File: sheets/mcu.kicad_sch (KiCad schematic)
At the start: 37 parts, among them SW1 SW_Nidec_CAS-120A1, SW2 SW_Push, U1 STM32H755ZIT6, Y1 25M, Y2 32k768

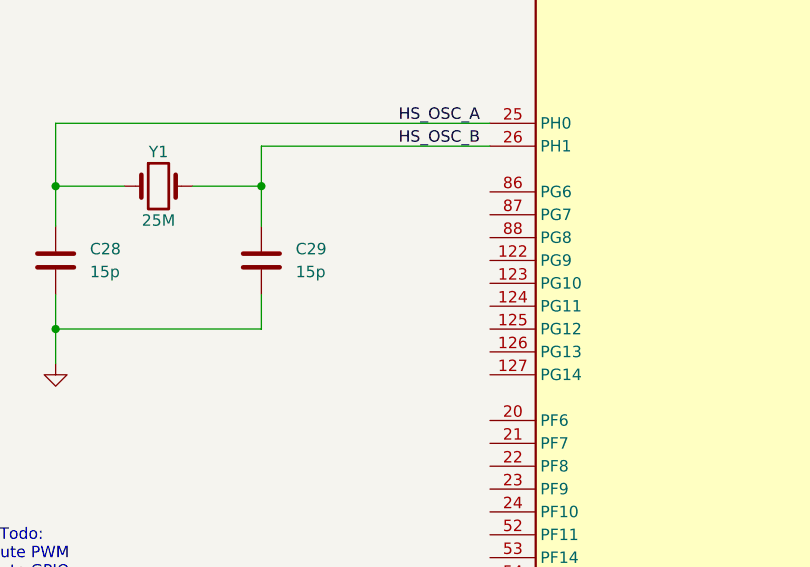
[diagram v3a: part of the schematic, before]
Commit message: assigned gpio pin to led (pg6)
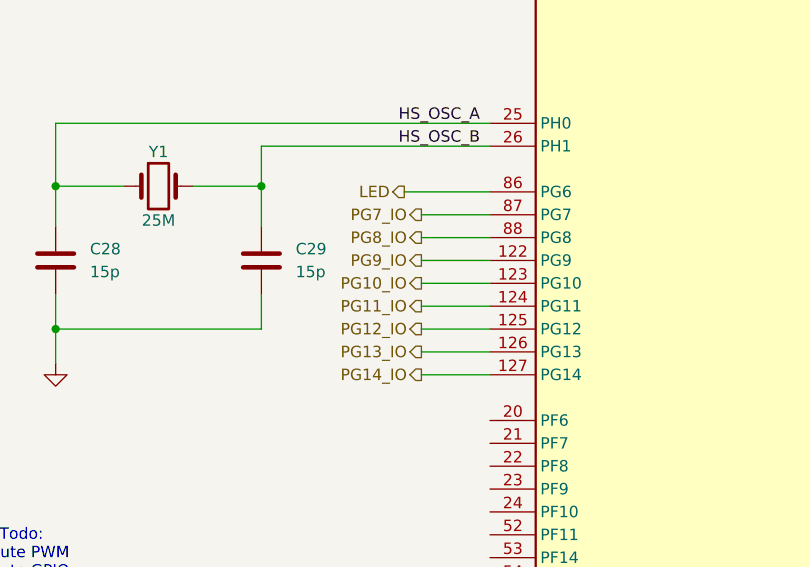
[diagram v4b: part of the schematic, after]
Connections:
- net PG9_IO: now reaches U1.122 (PG9)
- net PG10_IO: now reaches U1.123 (PG10)
- net PG11_IO: now reaches U1.124 (PG11)
- net PG12_IO: now reaches U1.125 (PG12)
- net PG13_IO: now reaches U1.126 (PG13)
- net PG14_IO: now reaches U1.127 (PG14)
- net LED: now reaches U1.86 (PG6)
- net PG7_IO: now reaches U1.87 (PG7)
- net PG8_IO: now reaches U1.88 (PG8)
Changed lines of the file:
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@@
 	(wire
 		(pts
+			(xy 257.81 111.76) (xy 265.43 111.76)
+		)
+		(stroke
+			(width 0)
+			(type default)
+		)
+	)
+	(wire
+		(pts
 			(xy 351.79 81.28) (xy 356.87 81.28)
 		)
@@
 	(wire
 		(pts
+			(xy 257.81 116.84) (xy 265.43 116.84)
+		)
+		(stroke
+			(width 0)
+			(type default)
+		)
+	)
+	(wire
+		(pts
 			(xy 129.54 82.55) (xy 132.08 82.55)
 		)
@@
 	(wire
 		(pts
+			(xy 257.81 121.92) (xy 265.43 121.92)
+		)
+		(stroke
+			(width 0)
+			(type default)
+		)
+	)
+	(wire
+		(pts
 			(xy 220.98 45.72) (xy 220.98 49.53)
 		)
@@
 	(wire
 		(pts
+			(xy 257.81 109.22) (xy 265.43 109.22)
+		)
+		(stroke
+			(width 0)
+			(type default)
+		)
+	)
+	(wire
+		(pts
 			(xy 351.79 142.24) (xy 366.395 142.24)
 		)
@@
 	(wire
 		(pts
+			(xy 257.81 119.38) (xy 265.43 119.38)
+		)
+		(stroke
+			(width 0)
+			(type default)
+		)
+	)
+	(wire
+		(pts
 			(xy 130.81 26.67) (xy 130.81 27.94)
 		)
@@
 	(wire
 		(pts
+			(xy 257.81 106.68) (xy 265.43 106.68)
+		)
+		(stroke
+			(width 0)
+			(type default)
+		)
+	)
+	(wire
+		(pts
 			(xy 109.22 82.55) (xy 109.22 86.36)
 		)
@@
 		)
 	)
+	(wire
+		(pts
+			(xy 257.81 124.46) (xy 265.43 124.46)
+		)
+		(stroke
+			(width 0)
+			(type default)
+		)
+	)
 	(bus
 		(pts
@@
 	(wire
 		(pts
+			(xy 257.81 114.3) (xy 265.43 114.3)
+		)
+		(stroke
+			(width 0)
+			(type default)
+		)
+	)
+	(wire
+		(pts
 			(xy 62.23 24.13) (xy 50.8 24.13)
 		)
@@
 	(wire
 		(pts
+			(xy 255.905 104.14) (xy 265.43 104.14)
+		)
+		(stroke
+			(width 0)
+			(type default)
+		)
+	)
+	(wire
+		(pts
 			(xy 109.22 82.55) (xy 111.76 82.55)
 		)
@@
 		)
 	)
+	(hierarchical_label "PG8_IO"
+		(shape output)
+		(at 257.81 109.22 180)
+		(effects
+			(font
+				(size 1.27 1.27)
+			)
+			(justify right)
+		)
+	)
 	(hierarchical_label "NEOM9N_EXTI0"
 		(shape input)
@@
 		)
 	)
+	(hierarchical_label "PG11_IO"
+		(shape output)
+		(at 257.81 116.84 180)
+		(effects
+			(font
+				(size 1.27 1.27)
+			)
+			(justify right)
+		)
+	)
 	(hierarchical_label "ADXL345{CS, SCLK, SDI, SDO, INT}"
 		(shape bidirectional)
@@
 		)
 	)
+	(hierarchical_label "PG10_IO"
+		(shape output)
+		(at 257.81 114.3 180)
+		(effects
+			(font
+				(size 1.27 1.27)
+			)
+			(justify right)
+		)
+	)
 	(hierarchical_label "LED_R"
 		(shape output)
@@
 		)
 	)
+	(hierarchical_label "LED"
+		(shape output)
+		(at 255.905 104.14 180)
+		(effects
+			(font
+				(size 1.27 1.27)
+			)
+			(justify right)
+		)
+	)
 	(hierarchical_label "SPARE_ADC1"
 		(shape input)
@@
 		)
 	)
+	(hierarchical_label "PG12_IO"
+		(shape output)
+		(at 257.81 119.38 180)
+		(effects
+			(font
+				(size 1.27 1.27)
+			)
+			(justify right)
+		)
+	)
 	(hierarchical_label "USB_D_P"
 		(shape bidirectional)
@@
 		)
 	)
+	(hierarchical_label "PG14_IO"
+		(shape output)
+		(at 257.81 124.46 180)
+		(effects
+			(font
+				(size 1.27 1.27)
+			)
+			(justify right)
+		)
+	)
+	(hierarchical_label "PG9_IO"
+		(shape output)
+		(at 257.81 111.76 180)
+		(effects
+			(font
+				(size 1.27 1.27)
+			)
+			(justify right)
+		)
+	)
 	(hierarchical_label "AIRBRAKE_POT1"
 		(shape input)
@@
 		)
 	)
+	(hierarchical_label "PG7_IO"
+		(shape output)
+		(at 257.81 106.68 180)
+		(effects
+			(font
+				(size 1.27 1.27)
+			)
+			(justify right)
+		)
+	)
+	(hierarchical_label "PG13_IO"
+		(shape output)
+		(at 257.81 121.92 180)
+		(effects
+			(font
+				(size 1.27 1.27)
+			)
+			(justify right)
+		)
+	)

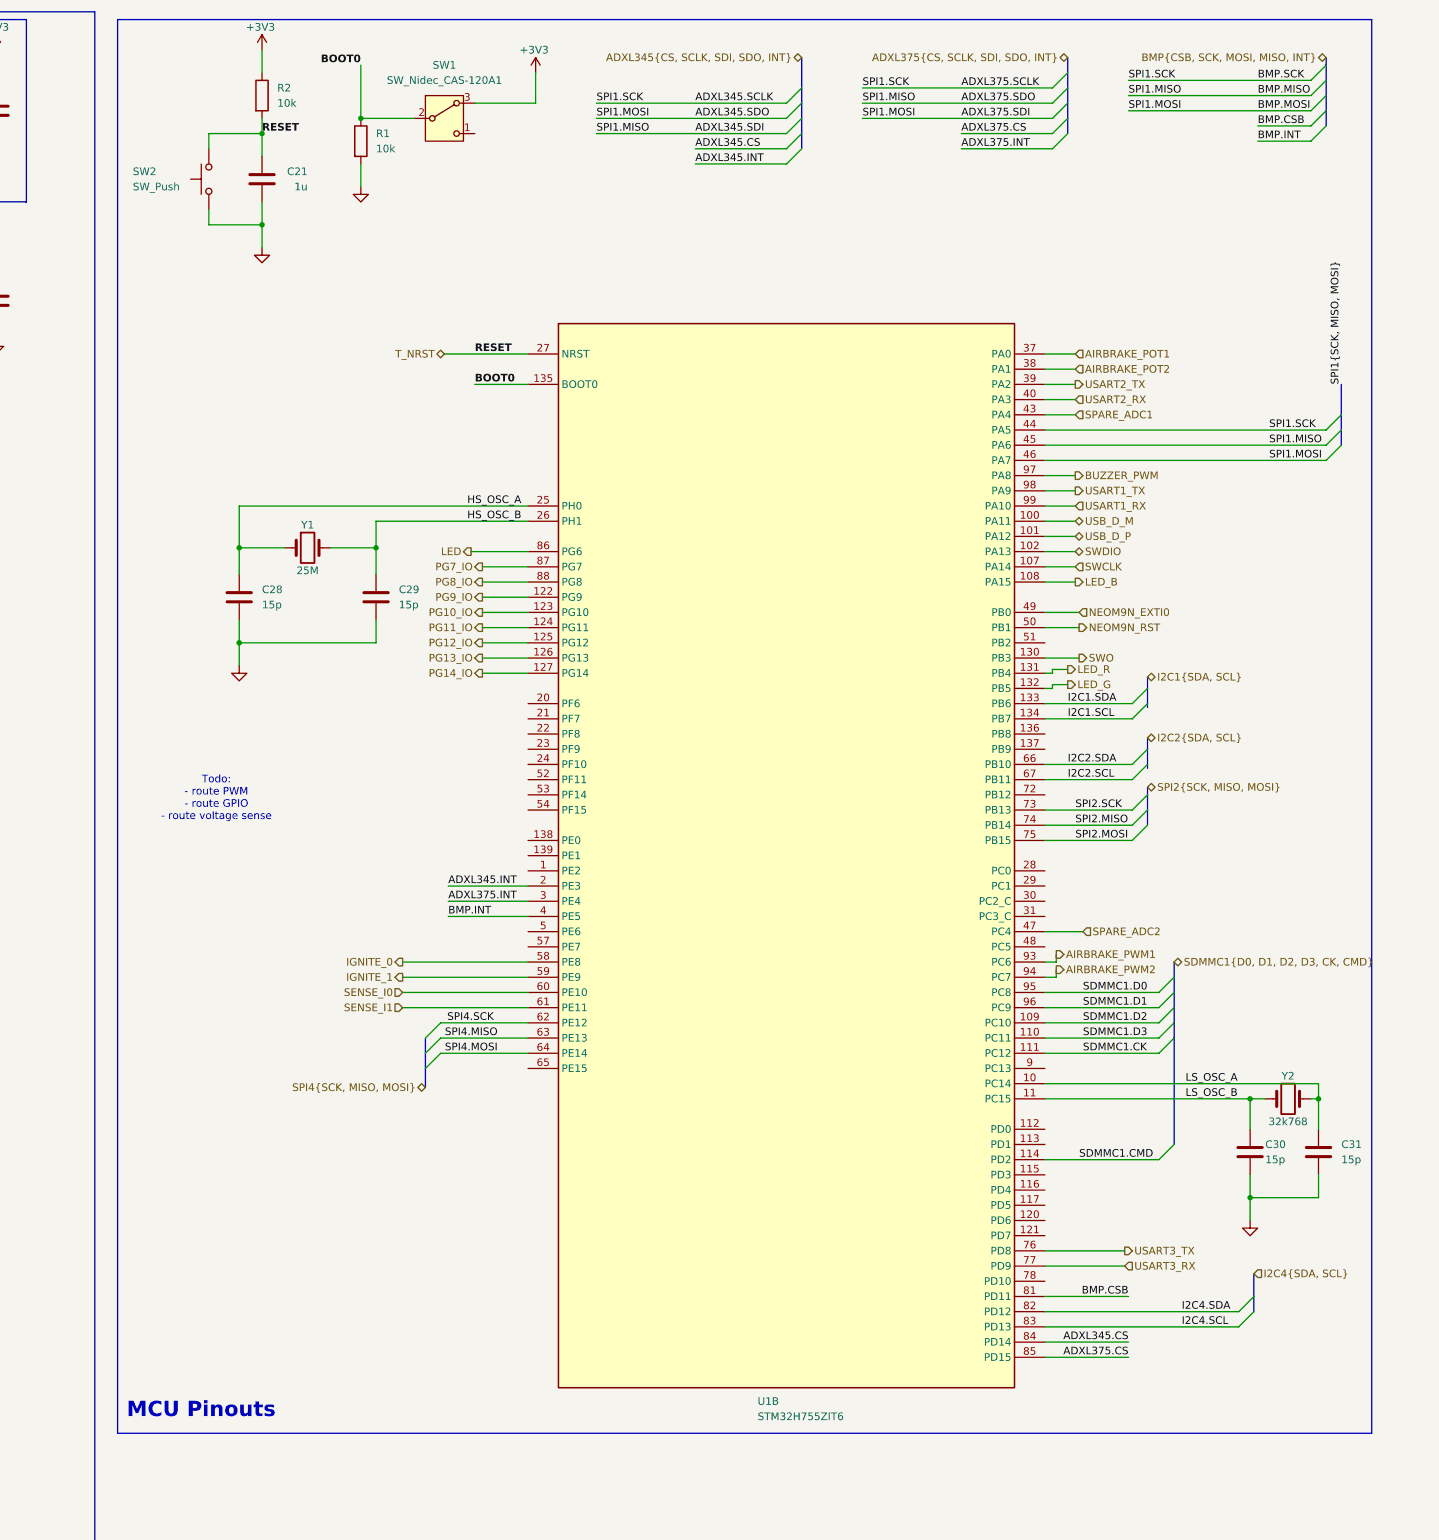
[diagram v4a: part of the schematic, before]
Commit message: added gpio connections in root, UART8, ADC2
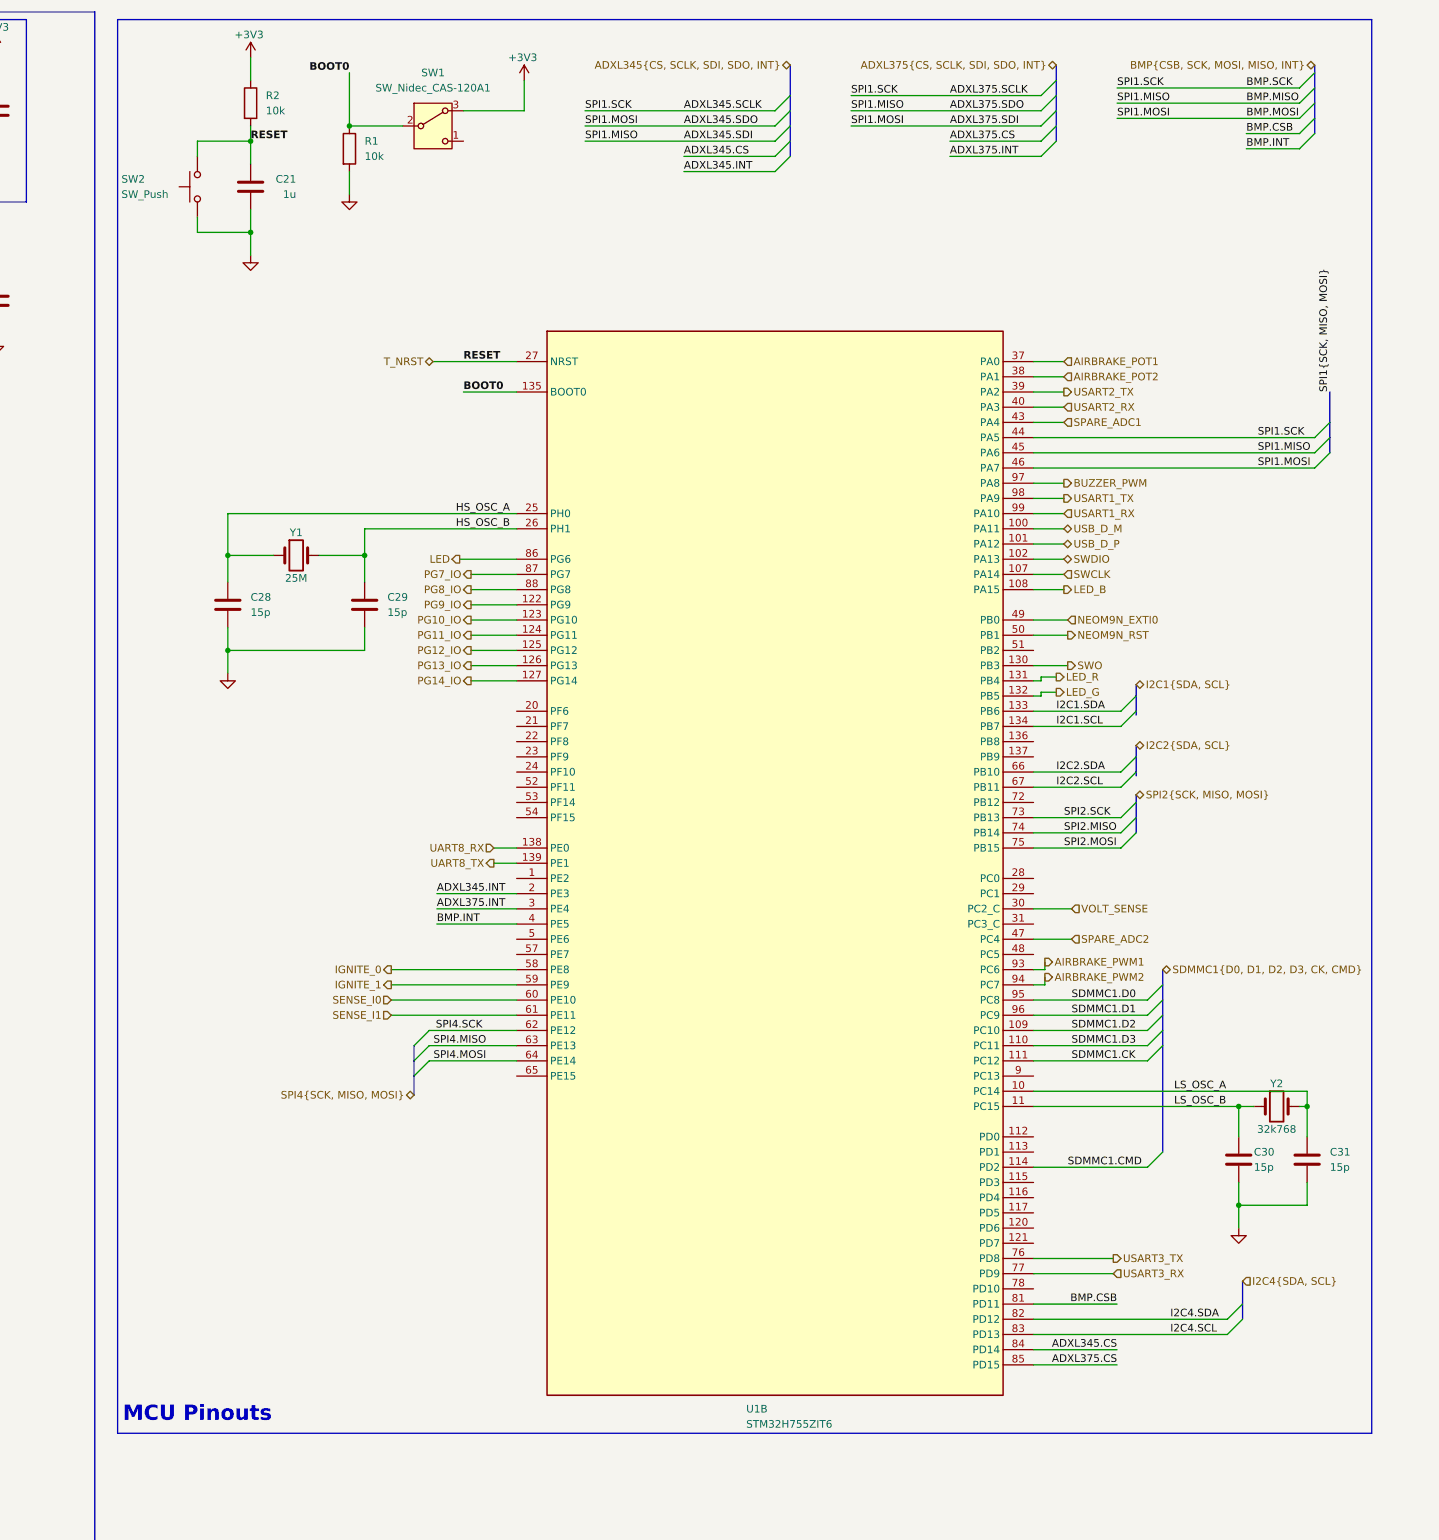
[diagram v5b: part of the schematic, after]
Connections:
- net UART8_RX: now reaches U1.138 (PE0)
- net UART8_TX: now reaches U1.139 (PE1)
- net VOLT_SENSE: now reaches U1.30 (PC2_C)
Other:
- note removed: "Todo: - route PWM - route GPIO - route voltage sense"
- moved on the sheet: C21, C28, C29, C30, C31, R1, R2, SW1, SW2, U1B, Y1, Y2

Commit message: final pwm channels added
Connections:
- net PWM1: now reaches U1.5 (PE6)
- net PWM2: now reaches U1.57 (PE7)
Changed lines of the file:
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@@
 		)
 	)
+	(wire
+		(pts
+			(xy 257.81 168.91) (xy 263.525 168.91)
+		)
+		(stroke
+			(width 0)
+			(type default)
+		)
+	)
 	(bus
 		(pts
@@
 	(wire
 		(pts
+			(xy 257.81 171.45) (xy 263.525 171.45)
+		)
+		(stroke
+			(width 0)
+			(type default)
+		)
+	)
+	(wire
+		(pts
 			(xy 153.67 24.13) (xy 142.24 24.13)
 		)
@@
 		)
 	)
+	(hierarchical_label "PWM2"
+		(shape output)
+		(at 257.81 171.45 180)
+		(effects
+			(font
+				(size 1.27 1.27)
+			)
+			(justify right)
+		)
+	)
 	(hierarchical_label "BMP{CSB, SCK, MOSI, MISO, INT}"
 		(shape bidirectional)
@@
 		(effects
 			(font
+				(size 1.27 1.27)
+			)
+			(justify right)
+		)
+	)
+	(hierarchical_label "PWM1"
+		(shape output)
+		(at 257.81 168.91 180)
+		(effects
+			(font

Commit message: Rev1 schematic done
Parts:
- removed SW1: SW_Nidec_CAS-120A1, Button_Switch_SMD:Nidec_Copal_CAS-120A, symbol Switch:SW_Nidec_CAS-120A1
- added SW2: SW_SPST, symbol Switch:SW_SPST
- renumbered C15 to C1, C9 to C10, C8 to C11, C7 to C12, C6 to C13, C5 to C14, C18 to C15, C4 to C16, C3 to C17, C16 to C18, C14 to C2, C2 to C20, C1 to C21, C20 to C22, C28 to C23, C21 to C24, C29 to C25, C30 to C26, C31 to C27, C17 to C3, C13 to C4, C12 to C5, C22 to C6, C23 to C7, C11 to C8, C10 to C9, R3 to R1, R1 to R3, SW2 to SW1
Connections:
- net +3V3: now also SW2.2 (B)
- net BOOT0: now also SW2.1 (A)
- no-connect marks 0 -> 27
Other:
- moved on the sheet: C23, C24, C25, C26, C27, C6, C7, R2, R3, SW1, U1B, Y1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
